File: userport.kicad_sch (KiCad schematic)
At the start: 41 parts, among them J3 C64_User_Port, J4 Mini-DIN-8-With-Shield, J5 C64_Tape_Port, J6 OKR-T/3-W12-C, U1 74LS595, U10 74LS125, U11 74LS595, U2 74LVC165, U3 74LS125, U4 74LS595, U5 74LVC165, U6 74LS595, U7 74LVC165, U8 74LS125, U9 74LS125

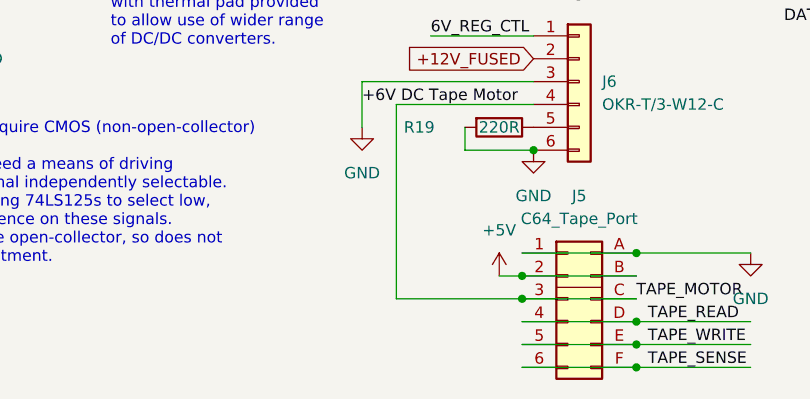
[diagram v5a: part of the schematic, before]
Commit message: add pullups for TAPE_SENSE and TAPE_READ
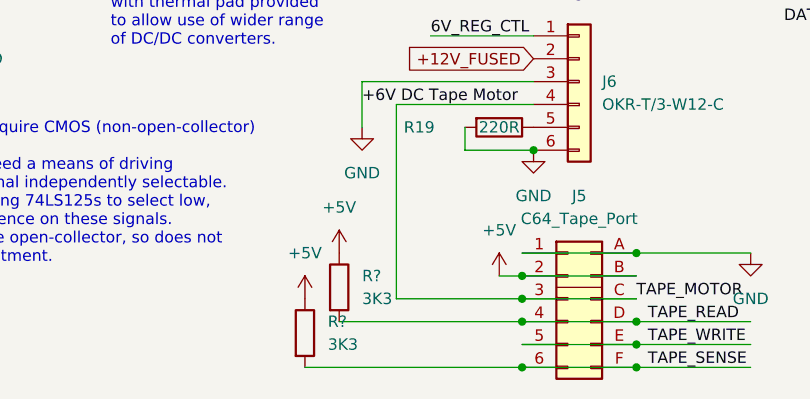
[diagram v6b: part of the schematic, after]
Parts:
- added R? (x2): 3K3, snapeda:Labeled Resistor, symbol Device:R
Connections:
- net +5V: now also R?.1, R?.1
- net TAPE_READ: now also R?.2
- net TAPE_SENSE: now also R?.2
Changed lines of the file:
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@@
   (junction (at 148.59 185.42) (diameter 0) (color 0 0 0 0)
   )
+  (junction (at 148.59 193.04) (diameter 0) (color 0 0 0 0)
+  )
+  (junction (at 148.59 187.96) (diameter 0) (color 0 0 0 0)
+  )
   (junction (at 148.59 182.88) (diameter 0) (color 0 0 0 0)
   )
@@
     (stroke (width 0) (type default) (color 0 0 0 0))
   )
+  (wire (pts (xy 148.59 187.96) (xy 161.29 187.96))
+    (stroke (width 0) (type default) (color 0 0 0 0))
+  )
   (wire (pts (xy 62.23 172.72) (xy 69.85 172.72))
     (stroke (width 0) (type default) (color 0 0 0 0))
@@
     (stroke (width 0) (type default) (color 0 0 0 0))
   )
-  (wire (pts (xy 148.59 187.96) (xy 161.29 187.96))
-    (stroke (width 0) (type default) (color 0 0 0 0))
-  )
   (wire (pts (xy 62.23 185.42) (xy 69.85 185.42))
     (stroke (width 0) (type default) (color 0 0 0 0))
@@
     (stroke (width 0) (type default) (color 0 0 0 0))
   )
+  (wire (pts (xy 124.46 193.04) (xy 148.59 193.04))
+    (stroke (width 0) (type default) (color 0 0 0 0))
+  )
   (wire (pts (xy 58.42 125.73) (xy 58.42 123.19))
     (stroke (width 0) (type default) (color 0 0 0 0))
@@
     (stroke (width 0) (type default) (color 0 0 0 0))
   )
-  (wire (pts (xy 148.59 193.04) (xy 161.29 193.04))
-    (stroke (width 0) (type default) (color 0 0 0 0))
-  )
   (wire (pts (xy 83.82 85.09) (xy 83.82 73.66))
     (stroke (width 0) (type default) (color 0 0 0 0))
@@
     (stroke (width 0) (type default) (color 0 0 0 0))
   )
+  (wire (pts (xy 128.27 187.96) (xy 148.59 187.96))
+    (stroke (width 0) (type default) (color 0 0 0 0))
+  )
   (wire (pts (xy 73.66 95.25) (xy 88.9 95.25))
     (stroke (width 0) (type default) (color 0 0 0 0))
@@
     (stroke (width 0) (type default) (color 0 0 0 0))
   )
+  (wire (pts (xy 148.59 193.04) (xy 161.29 193.04))
+    (stroke (width 0) (type default) (color 0 0 0 0))
+  )
   (wire (pts (xy 148.59 180.34) (xy 161.29 180.34))
     (stroke (width 0) (type default) (color 0 0 0 0))
@@
     (pin "2")
   )
+  (symbol (lib_id "Device:R") (at 128.27 184.15 0) (unit 1)
+    (in_bom yes) (on_board yes) (fields_autoplaced)
+    (property "Reference" "R?" (id 0) (at 130.81 182.8799 0)
+      (effects (font (size 1.27 1.27)) (justify left))
+    )
+    (property "Value" "3K3" (id 1) (at 130.81 185.4199 0)
+      (effects (font (size 1.27 1.27)) (justify left))
+    )
+    (property "Footprint" "snapeda:Labeled Resistor" (id 2) (at 126.492 184.15 90)
+      (effects (font (size 1.27 1.27)) hide)
+    )
+    (property "Datasheet" "~" (id 3) (at 128.27 184.15 0)
+      (effects (font (size 1.27 1.27)) hide)
+    )
+    (pin "1")
+    (pin "2")
+  )
   (symbol (lib_id "74xx:74LS125") (at 259.08 95.25 0) (unit 1)
     (in_bom yes) (on_board yes) (fields_autoplaced)
@@
     (pin "1")
   )
+  (symbol (lib_id "power:+5V") (at 124.46 185.42 0) (unit 1)
+    (in_bom yes) (on_board yes) (fields_autoplaced)
+    (property "Reference" "#PWR?" (id 0) (at 124.46 189.23 0)
+      (effects (font (size 1.27 1.27)) hide)
+    )
+    (property "Value" "+5V" (id 1) (at 124.46 180.34 0))
+    (property "Footprint" "" (id 2) (at 124.46 185.42 0)
+      (effects (font (size 1.27 1.27)) hide)
+    )
+    (property "Datasheet" "" (id 3) (at 124.46 185.42 0)
+      (effects (font (size 1.27 1.27)) hide)
+    )
+    (pin "1")
+  )
   (symbol (lib_id "power:GND") (at 62.23 187.96 0) (unit 1)
     (in_bom yes) (on_board yes) (fields_autoplaced)
@@
     (pin "13")
   )
+  (symbol (lib_id "Device:R") (at 124.46 189.23 0) (unit 1)
+    (in_bom yes) (on_board yes) (fields_autoplaced)
+    (property "Reference" "R?" (id 0) (at 127 187.9599 0)
+      (effects (font (size 1.27 1.27)) (justify left))
+    )
+    (property "Value" "3K3" (id 1) (at 127 190.4999 0)
+      (effects (font (size 1.27 1.27)) (justify left))
+    )
+    (property "Footprint" "snapeda:Labeled Resistor" (id 2) (at 122.682 189.23 90)
+      (effects (font (size 1.27 1.27)) hide)
+    )
+    (property "Datasheet" "~" (id 3) (at 124.46 189.23 0)
+      (effects (font (size 1.27 1.27)) hide)
+    )
+    (pin "1")
+    (pin "2")
+  )
   (symbol (lib_id "power:+5V") (at 138.43 115.57 0) (unit 1)
     (in_bom yes) (on_board yes) (fields_autoplaced)
@@
     (pin "N")
   )
+  (symbol (lib_id "power:+5V") (at 128.27 180.34 0) (unit 1)
+    (in_bom yes) (on_board yes) (fields_autoplaced)
+    (property "Reference" "#PWR?" (id 0) (at 128.27 184.15 0)
+      (effects (font (size 1.27 1.27)) hide)
+    )
+    (property "Value" "+5V" (id 1) (at 128.27 175.26 0))
+    (property "Footprint" "" (id 2) (at 128.27 180.34 0)
+      (effects (font (size 1.27 1.27)) hide)
+    )
+    (property "Datasheet" "" (id 3) (at 128.27 180.34 0)
+      (effects (font (size 1.27 1.27)) hide)
+    )
+    (pin "1")
+  )
   (symbol (lib_id "power:+5V") (at 209.55 113.03 0) (unit 1)
     (in_bom yes) (on_board yes) (fields_autoplaced)
@@
   (symbol (lib_id "power:GND") (at 173.99 180.34 0) (unit 1)
     (in_bom yes) (on_board yes) (fields_autoplaced)
-    (property "Reference" "#PWR?" (id 0) (at 173.99 186.69 0)
+    (property "Reference" "#PWR0101" (id 0) (at 173.99 186.69 0)
       (effects (font (size 1.27 1.27)) hide)
     )

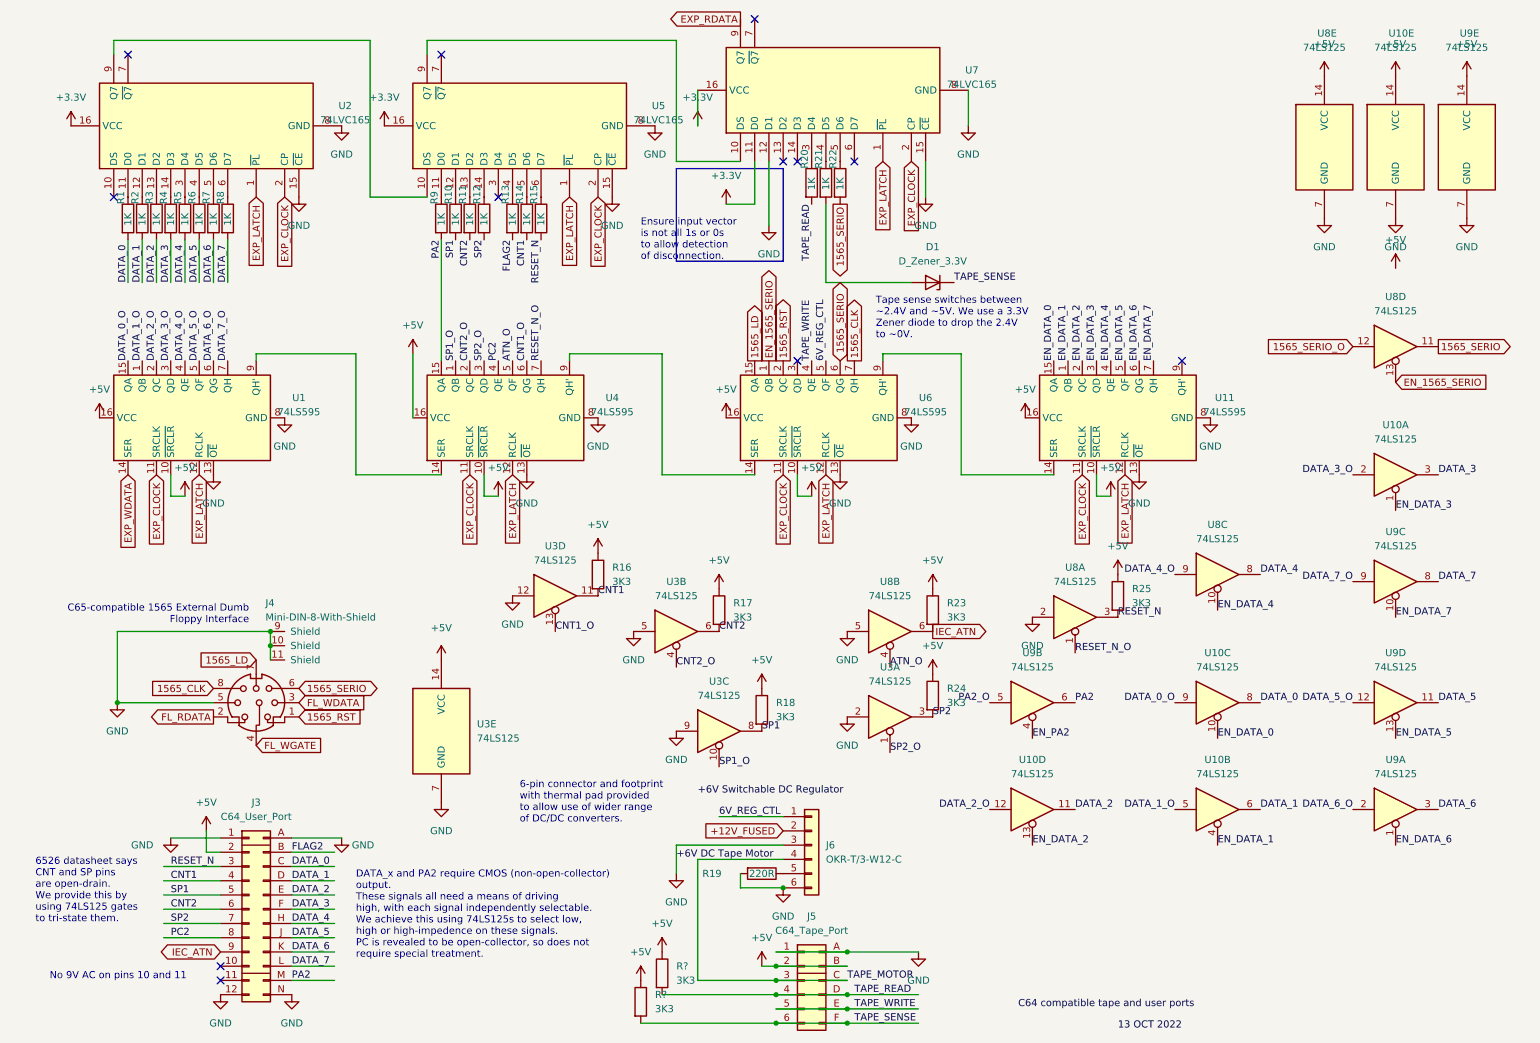
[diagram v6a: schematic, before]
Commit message: pull up tape inputs to 3.3V and get rid of zener diode
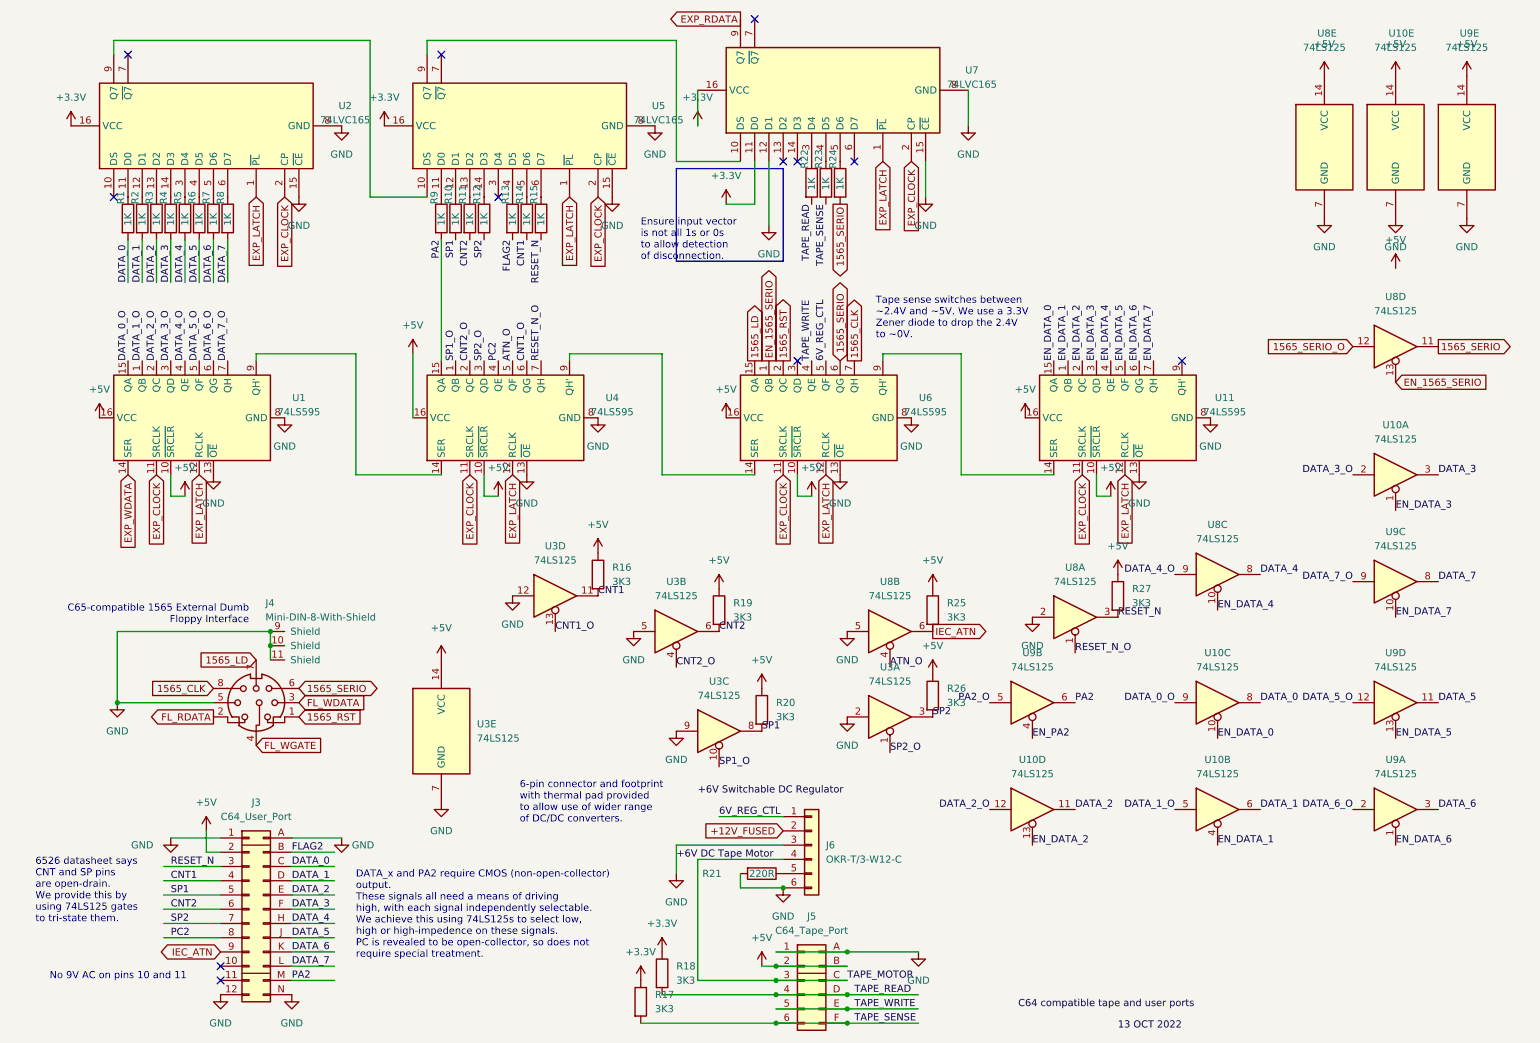
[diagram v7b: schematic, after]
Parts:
- removed D1: D_Zener_3.3V, Diode_THT:D_A-405_P10.16mm_Horizontal, symbol Device:D_Zener
- gave numbers to parts that had none: 2
- renumbered R17 to R19, R18 to R20, R19 to R21, R20 to R22, R21 to R23, R22 to R24, R23 to R25, R24 to R26, R25 to R27
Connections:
- net +3V3: now also R17.1, R18.1
- net +5V: no longer R17.1, R18.1
- net TAPE_SENSE: now also R23.2

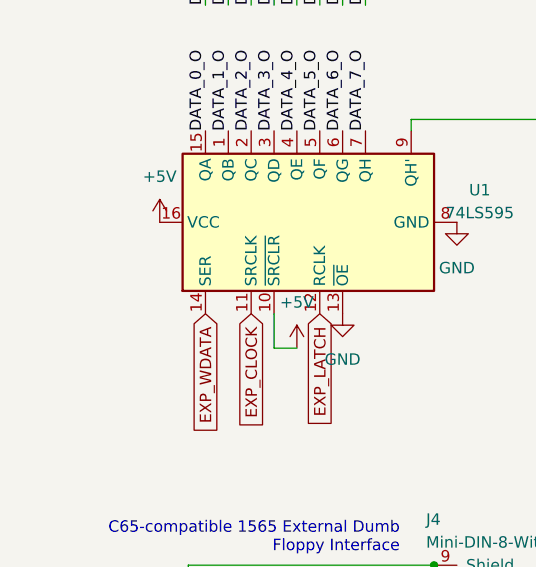
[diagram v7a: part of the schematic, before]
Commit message: add de-coupling cap to U1
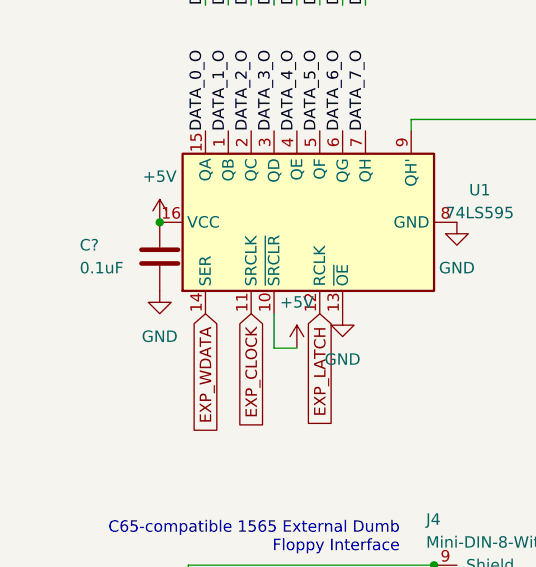
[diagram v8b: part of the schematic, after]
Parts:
- added C?: 0.1uF, Capacitor_THT:C_Disc_D10.0mm_W2.5mm_P5.00mm, symbol Device:C
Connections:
- net +5V: now also C?.1
- net GND: now also C?.2
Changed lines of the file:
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@@
   (junction (at 148.59 193.04) (diameter 0) (color 0 0 0 0)
   )
+  (junction (at 27.94 85.09) (diameter 0) (color 0 0 0 0)
+  )
   (junction (at 148.59 187.96) (diameter 0) (color 0 0 0 0)
   )
@@
     (pin "1")
   )
+  (symbol (lib_id "power:GND") (at 27.94 92.71 0) (unit 1)
+    (in_bom yes) (on_board yes) (fields_autoplaced)
+    (property "Reference" "#PWR?" (id 0) (at 27.94 99.06 0)
+      (effects (font (size 1.27 1.27)) hide)
+    )
+    (property "Value" "GND" (id 1) (at 27.94 97.79 0))
+    (property "Footprint" "" (id 2) (at 27.94 92.71 0)
+      (effects (font (size 1.27 1.27)) hide)
+    )
+    (property "Datasheet" "" (id 3) (at 27.94 92.71 0)
+      (effects (font (size 1.27 1.27)) hide)
+    )
+    (pin "1")
+  )
   (symbol (lib_id "power:+5V") (at 246.38 24.13 0) (unit 1)
     (in_bom yes) (on_board yes) (fields_autoplaced)
@@
   (symbol (lib_id "power:+3.3V") (at 124.46 185.42 0) (unit 1)
     (in_bom yes) (on_board yes) (fields_autoplaced)
-    (property "Reference" "#PWR?" (id 0) (at 124.46 189.23 0)
+    (property "Reference" "#PWR0101" (id 0) (at 124.46 189.23 0)
       (effects (font (size 1.27 1.27)) hide)
     )
@@
   (symbol (lib_id "power:+3.3V") (at 128.27 180.34 0) (unit 1)
     (in_bom yes) (on_board yes) (fields_autoplaced)
-    (property "Reference" "#PWR?" (id 0) (at 128.27 184.15 0)
+    (property "Reference" "#PWR0102" (id 0) (at 128.27 184.15 0)
       (effects (font (size 1.27 1.27)) hide)
     )
@@
     (pin "N")
   )
+  (symbol (lib_id "Device:C") (at 27.94 88.9 0) (unit 1)
+    (in_bom yes) (on_board yes)
+    (property "Reference" "C?" (id 0) (at 19.05 87.63 0)
+      (effects (font (size 1.27 1.27)) (justify left))
+    )
+    (property "Value" "0.1uF" (id 1) (at 19.05 90.17 0)
+      (effects (font (size 1.27 1.27)) (justify left))
+    )
+    (property "Footprint" "Capacitor_THT:C_Disc_D10.0mm_W2.5mm_P5.00mm" (id 2) (at 28.9052 92.71 0)
+      (effects (font (size 1.27 1.27)) hide)
+    )
+    (property "Datasheet" "~" (id 3) (at 27.94 88.9 0)
+      (effects (font (size 1.27 1.27)) hide)
+    )
+    (pin "1")
+    (pin "2")
+  )
   (symbol (lib_id "power:+5V") (at 209.55 113.03 0) (unit 1)
